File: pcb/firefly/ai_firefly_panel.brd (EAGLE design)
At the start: 20.3 x 20.3 mm, 10 parts, among them IC1 ATTINY45TINY85-SMT

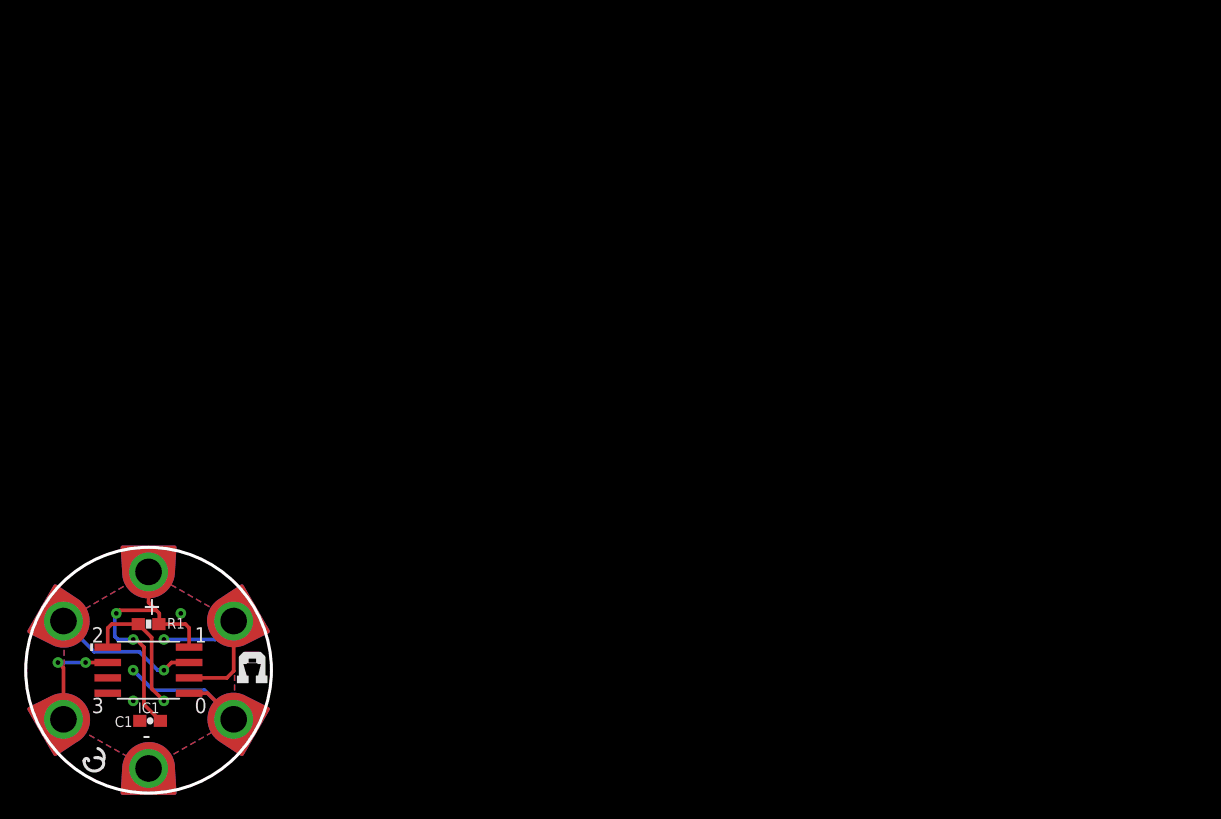
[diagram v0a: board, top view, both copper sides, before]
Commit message: updating pdf schematics
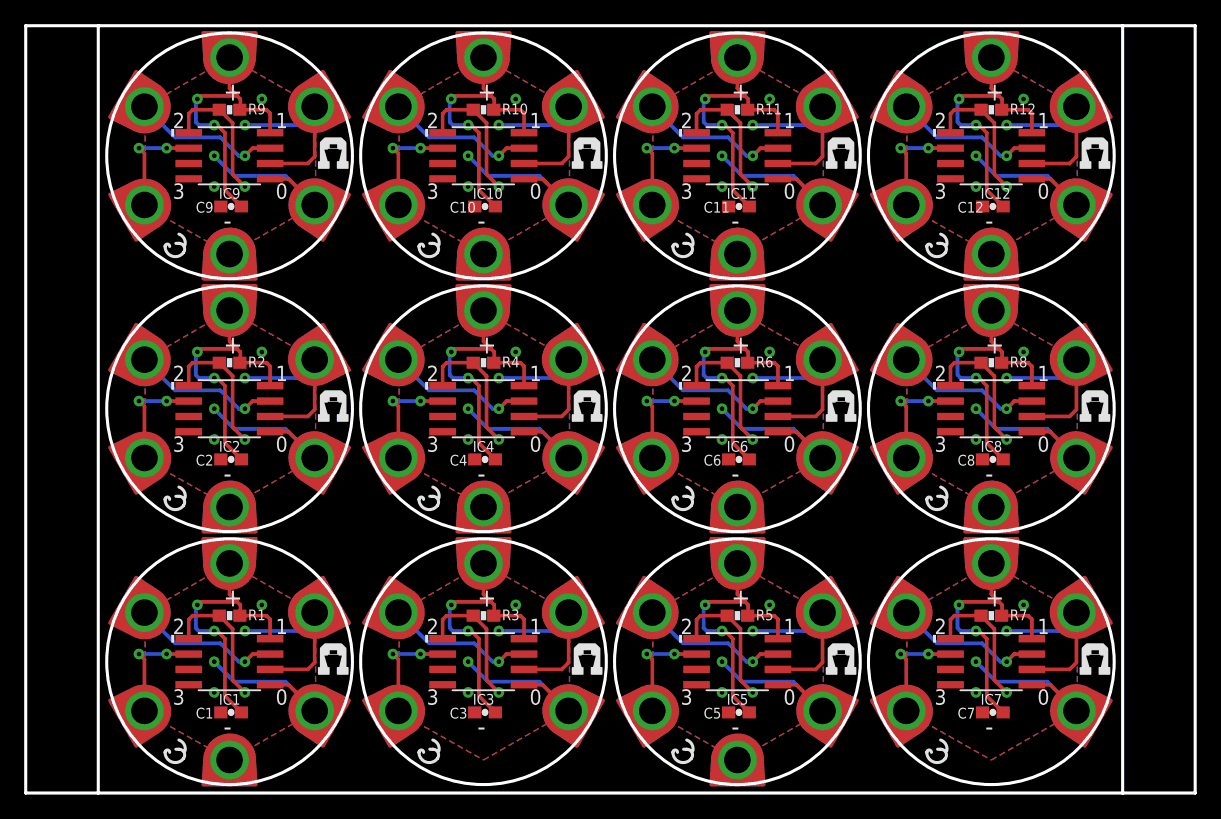
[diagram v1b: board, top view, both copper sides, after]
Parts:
- added +1, +10, +11, +2, +3, +4, +5, +6, +7, +8, +9, -1, -2, -3, -4, -5, -6, -7, -8, -9, 10, 11, 12, 13, 14, 15, 16, 17, 18, 19, 20, 21, 22, 23, 24, 25, 26, 27, 28, 29, 30, 31, 32, 33, 34, 35, 36, 37, 38, 39, 4, 40, 41, 42, 43, 44, 45, 46, 47, 5, 6, 7, 8, 9: 1X01-PETAL, Ai_Connectors:1X01-PETAL
- added C10, C11, C12, C2, C3, C4, C5, C6, C7, C8, C9: 0.1uF, Ai_Passives:CAP-0603
- added IC10, IC11, IC12, IC2, IC3, IC4, IC5, IC6, IC7, IC8, IC9: ATTINY45TINY85-SMT, Ai_IC:S008-EIAJ
- added R10, R11, R12, R2, R3, R4, R5, R6, R7, R8, R9: 10K, Ai_Passives:RES-0603
- added U$1, U$10, U$11, U$12, U$2, U$3, U$4, U$5, U$6, U$7, U$8: AI-LOGOXS, Ai_Miscellany:AI-LOGO-XS
- moved + 6.74 mm to (16.9, 19.0)
- moved - 6.74 mm to (16.9, 2.73)
- moved 0 6.74 mm to (23.9, 6.80)
- moved 1 6.74 mm to (23.9, 14.9)
- moved 2 6.74 mm to (9.82, 14.9)
- moved 3 6.74 mm to (9.82, 6.80)
- moved IC1 6.74 mm to (16.9, 10.9)
- moved R1 6.74 mm to (16.9, 14.7)
- moved U$9 6.74 mm to (24.1, 9.72)
- moved C1 6.74 mm to (17.0, 6.67)
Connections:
- new net 10: 8.1, IC3.6
- new net 11: 9.1, IC3.5
- new net 12: 14.1, IC4.2
- new net 13: 15.1, IC4.7
- new net 14: 12.1, IC4.6
- new net 15: 13.1, IC4.5
- new net 16: 18.1, IC5.2
- new net 17: 19.1, IC5.7
- new net 18: 16.1, IC5.6
- new net 19: 17.1, IC5.5
- new net 20: 22.1, IC6.2
- new net 21: 23.1, IC6.7
- new net 22: 20.1, IC6.6
- new net 23: 21.1, IC6.5
- new net 24: 26.1, IC7.2
- new net 25: 27.1, IC7.7
- new net 26: 24.1, IC7.6
- new net 27: 25.1, IC7.5
- new net 28: 30.1, IC8.2
- new net 29: 31.1, IC8.7
- new net 30: 28.1, IC8.6
- new net 31: 29.1, IC8.5
- new net 32: 34.1, IC9.2
- new net 33: 35.1, IC9.7
- new net 34: 32.1, IC9.6
- new net 35: 33.1, IC9.5
- new net 36: 38.1, IC10.2
- new net 37: 39.1, IC10.7
- new net 38: 36.1, IC10.6
- new net 39: 37.1, IC10.5
- new net 4: 6.1, IC2.2
- new net 40: 42.1, IC11.2
- new net 41: 43.1, IC11.7
- new net 42: 40.1, IC11.6
- new net 43: 41.1, IC11.5
- new net 44: 46.1, IC12.2
- new net 45: 47.1, IC12.7
- new net 46: 44.1, IC12.6
- new net 47: 45.1, IC12.5
- new net 5: 7.1, IC2.7
- new net 6: 4.1, IC2.6
- new net 7: 5.1, IC2.5
- new net 8: 10.1, IC3.2
- new net 9: 11.1, IC3.7
- new net GND1: -1.1, C2.2, IC2.4
- new net GND10: -8.1, C11.2, IC11.4
- new net GND11: -9.1, C12.2, IC12.4
- new net GND2: C3.2, IC3.4
- new net GND3: -2.1, C4.2, IC4.4
- new net GND4: -3.1, C5.2, IC5.4
- new net GND5: -4.1, C6.2, IC6.4
- new net GND6: C7.2, IC7.4
- new net GND7: -5.1, C8.2, IC8.4
- new net GND8: -6.1, C9.2, IC9.4
- new net GND9: -7.1, C10.2, IC10.4
- new net RES1: IC2.1, R2.1
- new net RES10: IC11.1, R11.1
- new net RES11: IC12.1, R12.1
- new net RES2: IC3.1, R3.1
- new net RES3: IC4.1, R4.1
- new net RES4: IC5.1, R5.1
- new net RES5: IC6.1, R6.1
- new net RES6: IC7.1, R7.1
- new net RES7: IC8.1, R8.1
- new net RES8: IC9.1, R9.1
- new net RES9: IC10.1, R10.1
- new net VCC1: +1.1, C2.1, IC2.8, R2.2
- new net VCC10: +10.1, C11.1, IC11.8, R11.2
- new net VCC11: +11.1, C12.1, IC12.8, R12.2
- new net VCC2: +2.1, C3.1, IC3.8, R3.2
- new net VCC3: +3.1, C4.1, IC4.8, R4.2
- new net VCC4: +4.1, C5.1, IC5.8, R5.2
- new net VCC5: +5.1, C6.1, IC6.8, R6.2
- new net VCC6: +6.1, C7.1, IC7.8, R7.2
- new net VCC7: +7.1, C8.1, IC8.8, R8.2
- new net VCC8: +8.1, C9.1, IC9.8, R9.2
- new net VCC9: +9.1, C10.1, IC10.8, R10.2
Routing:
- net VCC11: track 0.00 -> 23.8 mm, vias 0 -> 2
- net VCC8: track 0.00 -> 23.8 mm, vias 0 -> 2
- net VCC7: track 0.00 -> 23.8 mm, vias 0 -> 2
- net VCC6: track 0.00 -> 23.8 mm, vias 0 -> 2
- net VCC9: track 0.00 -> 23.8 mm, vias 0 -> 2
- net VCC10: track 0.00 -> 23.8 mm, vias 0 -> 2
- net VCC5: track 0.00 -> 23.8 mm, vias 0 -> 2
- net VCC3: track 0.00 -> 23.8 mm, vias 0 -> 2
- net VCC1: track 0.00 -> 23.8 mm, vias 0 -> 2
- net VCC4: track 0.00 -> 23.8 mm, vias 0 -> 2
- net VCC2: track 0.00 -> 23.8 mm, vias 0 -> 2
- net 47: track 0.00 -> 14.6 mm, vias 0 -> 1
- net 31: track 0.00 -> 14.6 mm, vias 0 -> 1
- net 27: track 0.00 -> 14.6 mm, vias 0 -> 1
- net 23: track 0.00 -> 14.6 mm, vias 0 -> 1
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- added copper zone on layer 1, net GND1
- added copper zone on layer 16, net GND1
- added copper zone on layer 1, net GND10
- added copper zone on layer 16, net GND10
- added copper zone on layer 1, net GND11
- added copper zone on layer 16, net GND11
- added copper zone on layer 1, net GND2
- added copper zone on layer 16, net GND2
- added copper zone on layer 1, net GND3
- added copper zone on layer 16, net GND3
- added copper zone on layer 1, net GND4
- added copper zone on layer 16, net GND4
- added copper zone on layer 1, net GND5
- added copper zone on layer 16, net GND5
- added copper zone on layer 1, net GND6
- added copper zone on layer 16, net GND6
- added copper zone on layer 1, net GND7
- added copper zone on layer 16, net GND7
- added copper zone on layer 1, net GND8
- added copper zone on layer 16, net GND8
- added copper zone on layer 1, net GND9
- added copper zone on layer 16, net GND9
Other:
- board size 20.3 x 20.3 mm -> 96.7 x 63.5 mm
- board text added: "C1"
- board text added: "IC1"
- board text added: "Pasadena, CA"
- board text added: "R1"
